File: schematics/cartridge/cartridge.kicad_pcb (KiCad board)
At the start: 2 copper layers, 51 x 60.7 mm, 3 parts, among them J1 Pak_Connector, U1 AT28C256-15PU

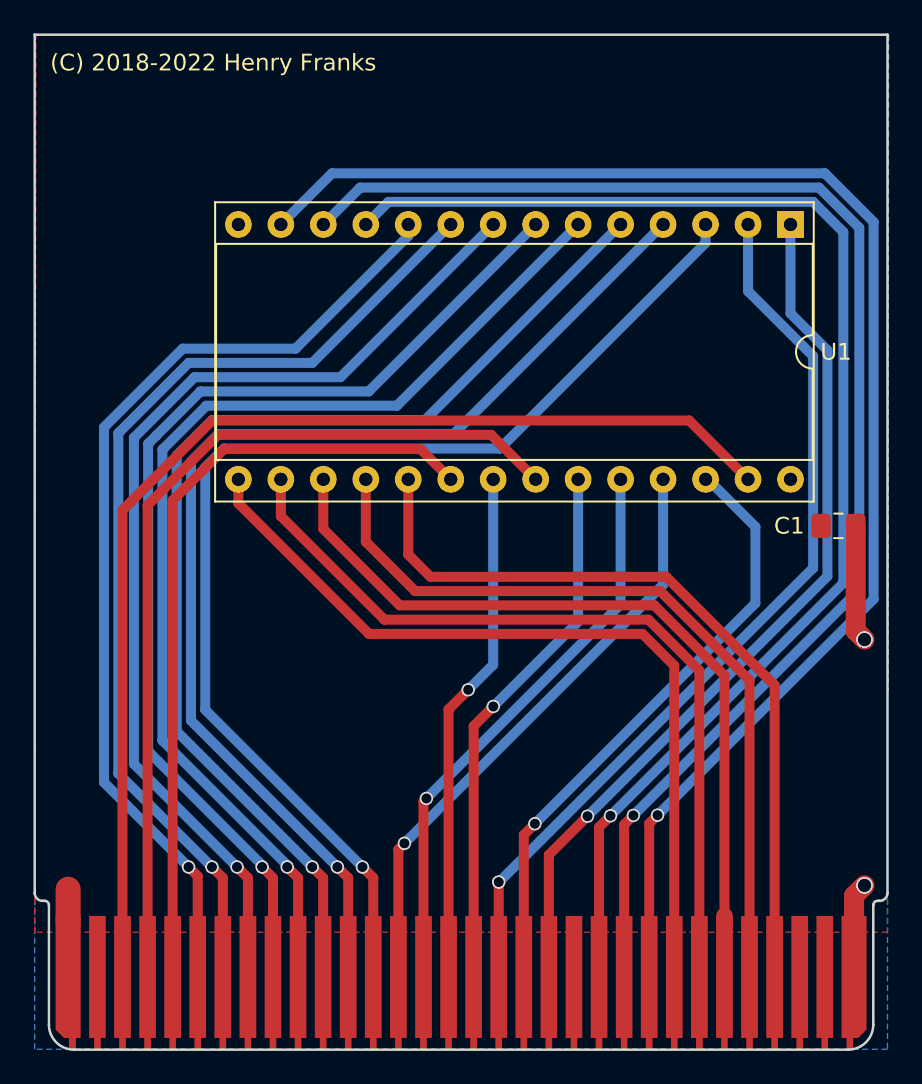
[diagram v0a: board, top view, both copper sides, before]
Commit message: Slightly edit silkscreen text for manufacture
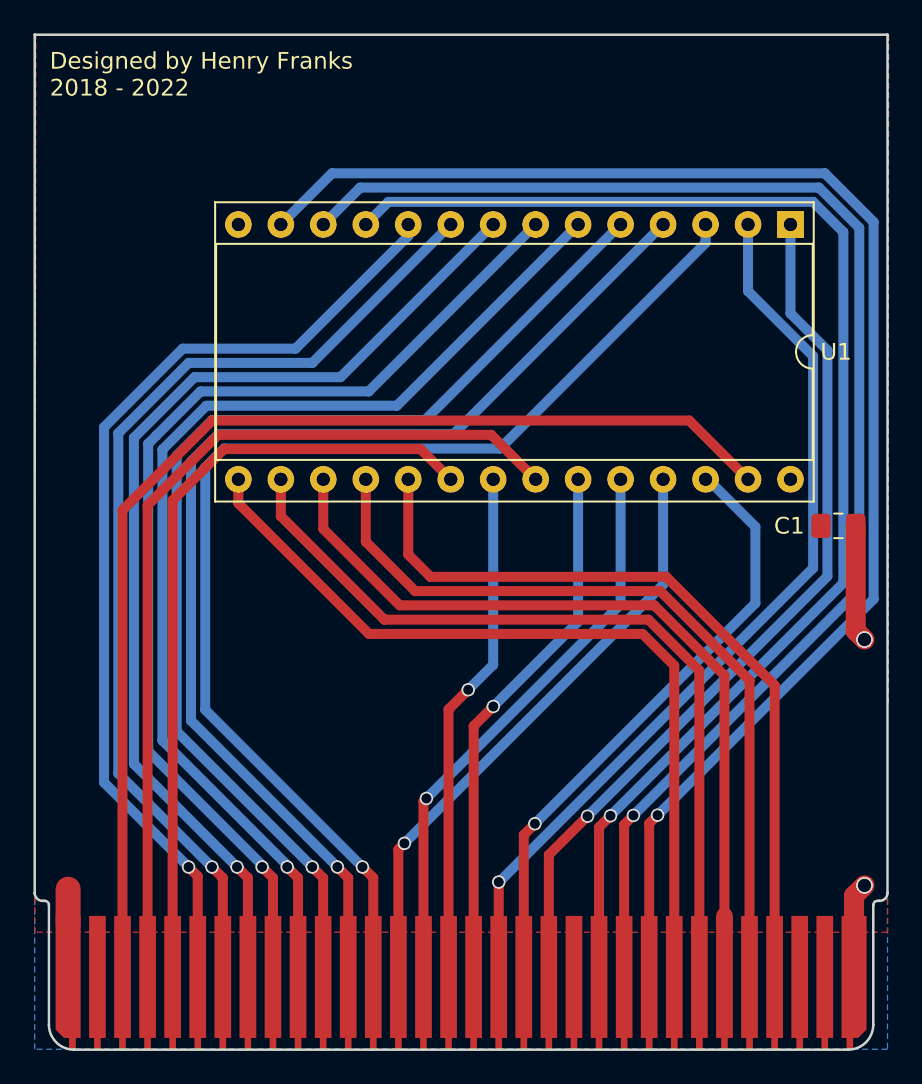
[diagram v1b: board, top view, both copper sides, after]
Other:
- rule pad_to_mask_clearance: 0.2 -> 0
- board text added: "Designed by Henry Franks 2018 - 2022"
- board text removed: "(C) 2018-2022 Henry Franks"
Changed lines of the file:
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@@
   )
   (setup
-    (pad_to_mask_clearance 0.2)
+    (stackup
+      (layer "F.SilkS" (type "Top Silk Screen"))
+      (layer "F.Paste" (type "Top Solder Paste"))
+      (layer "F.Mask" (type "Top Solder Mask") (thickness 0.01))
+      (layer "F.Cu" (type "copper") (thickness 0.035))
+      (layer "dielectric 1" (type "core") (thickness 1.51) (material "FR4") (epsilon_r 4.5) (loss_tangent 0.02))
+      (layer "B.Cu" (type "copper") (thickness 0.035))
+      (layer "B.Mask" (type "Bottom Solder Mask") (thickness 0.01))
+      (layer "B.Paste" (type "Bottom Solder Paste"))
+      (layer "B.SilkS" (type "Bottom Silk Screen"))
+      (copper_finish "None")
+      (dielectric_constraints no)
+    )
+    (pad_to_mask_clearance 0)
     (pcbplotparams
       (layerselection 0x00010fc_ffffffff)
       (disableapertmacros false)
-      (usegerberextensions false)
+      (usegerberextensions true)
       (usegerberattributes false)
       (usegerberadvancedattributes false)
@@
       (psa4output false)
       (plotreference true)
-      (plotvalue true)
+      (plotvalue false)
       (plotinvisibletext false)
       (sketchpadsonfab false)
-      (subtractmaskfromsilk false)
+      (subtractmaskfromsilk true)
       (outputformat 1)
       (mirror false)
-      (drillshape 1)
+      (drillshape 0)
       (scaleselection 1)
-      (outputdirectory "")
+      (outputdirectory "plot")
     )
   )
@@
     (fp_line (start -1 0.625) (end -1 -0.625) (layer "F.Fab") (width 0.1))
     (fp_line (start -1 -0.625) (end 1 -0.625) (layer "F.Fab") (width 0.1))
-    (pad "1" smd roundrect locked (at -1.0375 0) (size 1.175 1.45) (layers "F.Cu" "F.Paste" "F.Mask") (roundrect_rratio 0.212766)
+    (pad "1" smd roundrect locked (at -1.0375 0) (size 1.175 1.45) (layers "F.Cu" "F.Paste" "F.Mask") (roundrect_rratio 0.2127659574)
       (net 32 "5V"))
-    (pad "2" smd roundrect locked (at 1.0375 0) (size 1.175 1.45) (layers "F.Cu" "F.Paste" "F.Mask") (roundrect_rratio 0.212766)
+    (pad "2" smd roundrect locked (at 1.0375 0) (size 1.175 1.45) (layers "F.Cu" "F.Paste" "F.Mask") (roundrect_rratio 0.2127659574)
       (net 1 "GND"))
     (model "${KISYS3DMOD}/Capacitor_SMD.3dshapes/C_0805_2012Metric.wrl"
@@
   (gr_arc (start 124.475 117.125) (mid 124.139124 116.985876) (end 124 116.65) (layer "Edge.Cuts") (width 0.15))
   (gr_line (start 175 116.65) (end 175 65.325) (layer "Edge.Cuts") (width 0.15))
-  (gr_text "(C) 2018-2022 Henry Franks" (at 124.925 67) (layer "F.SilkS")
+  (gr_text "Designed by Henry Franks\n2018 - 2022" (at 124.9 67.7) (layer "F.SilkS")
     (effects (font (size 1 1) (thickness 0.15)) (justify left))
   )
